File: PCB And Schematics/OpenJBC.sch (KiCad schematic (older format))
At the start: 31 parts

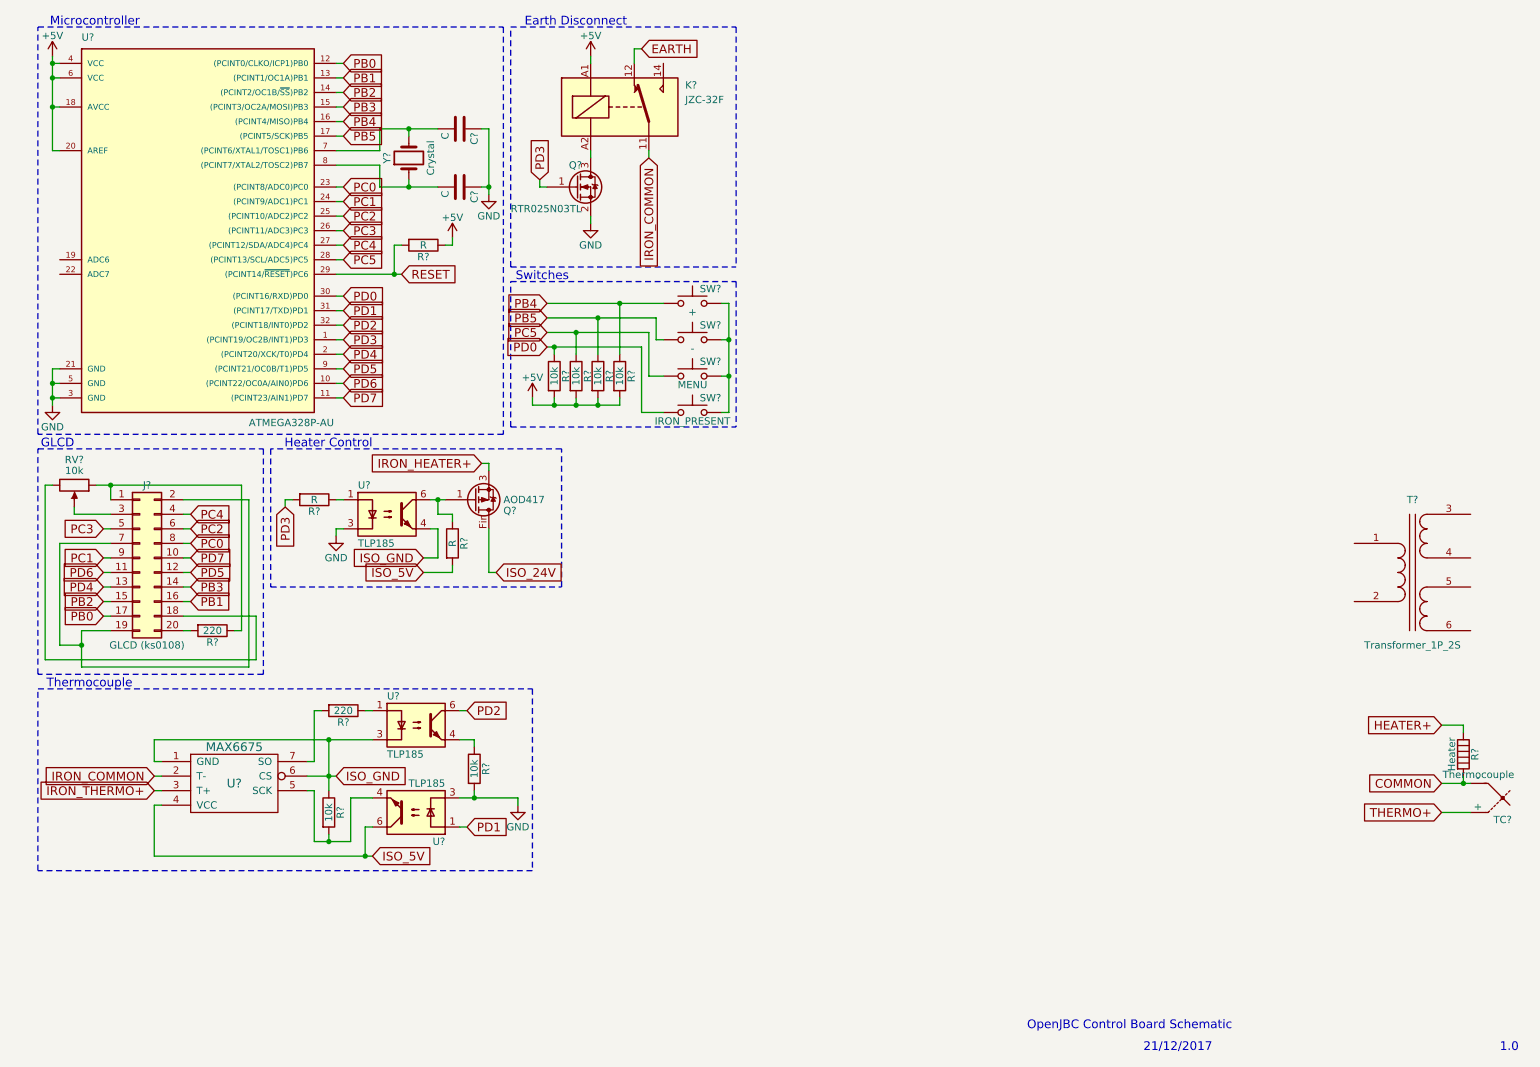
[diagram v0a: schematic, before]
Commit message: Created AVR Project and added some missing parts
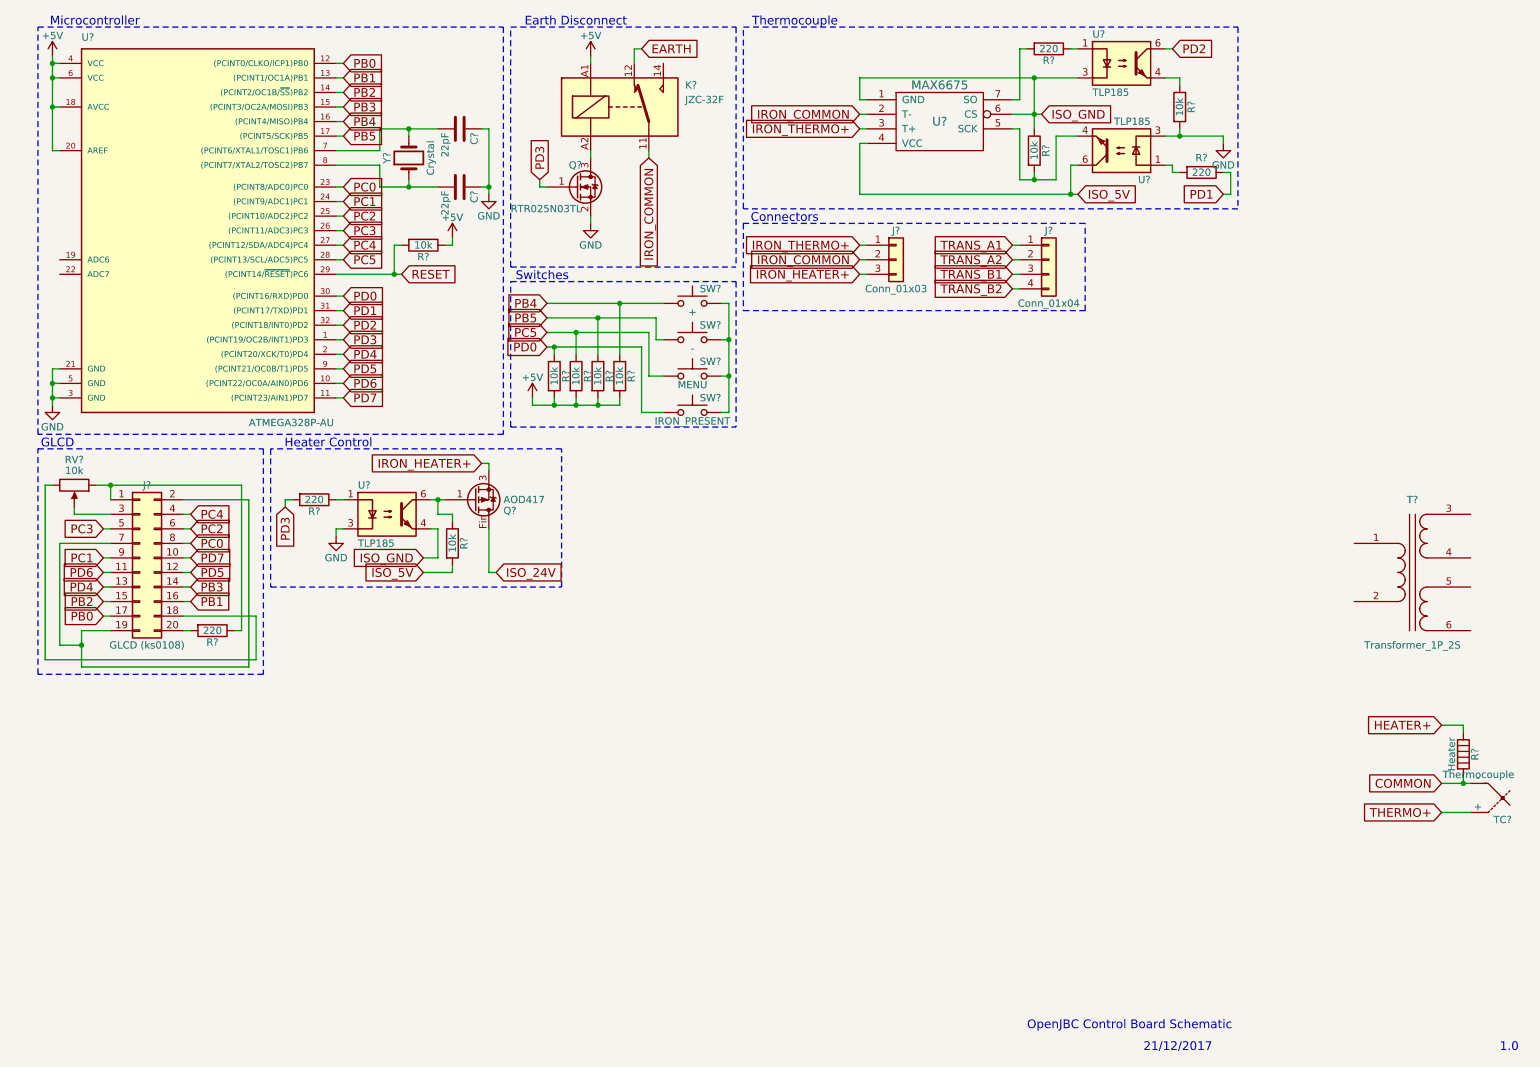
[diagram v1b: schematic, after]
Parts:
- added J?: Conn_01x03, symbol Conn_01x03
- added J?: Conn_01x04, symbol Conn_01x04
- added R?: 220, symbol R
- C? (x2): value C -> 22pF
- R? (x2): value R -> 10k
- R?: value R -> 220
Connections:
- net IRON_COMMON: now also J?.2 (Pin_2)
- net IRON_HEATER+: now also J?.3 (Pin_3)
- net IRON_THERMO+: now also J?.1 (Pin_1)
- net PD1: now also R?.1; no longer U?.1
- new net: R?.2, U?.1
- new net TRANS_A1: J?.1 (Pin_1)
- new net TRANS_A2: J?.2 (Pin_2)
- new net TRANS_B1: J?.3 (Pin_3)
- new net TRANS_B2: J?.4 (Pin_4)
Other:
- note added: "Connectors"
- moved on the sheet: R?, U?
